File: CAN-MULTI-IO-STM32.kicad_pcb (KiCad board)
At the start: 2 copper layers, 81 x 55 mm, 63 parts, among them J1 H GND L, J2 TERM, J3 USART1, J5 PWR IN, U1 STM32L433RCT3, U2 MCP2562-E-SN, U3 LMR54410, U4 ADS1015IDGS, U5 PCA9537, U6 TCA9511

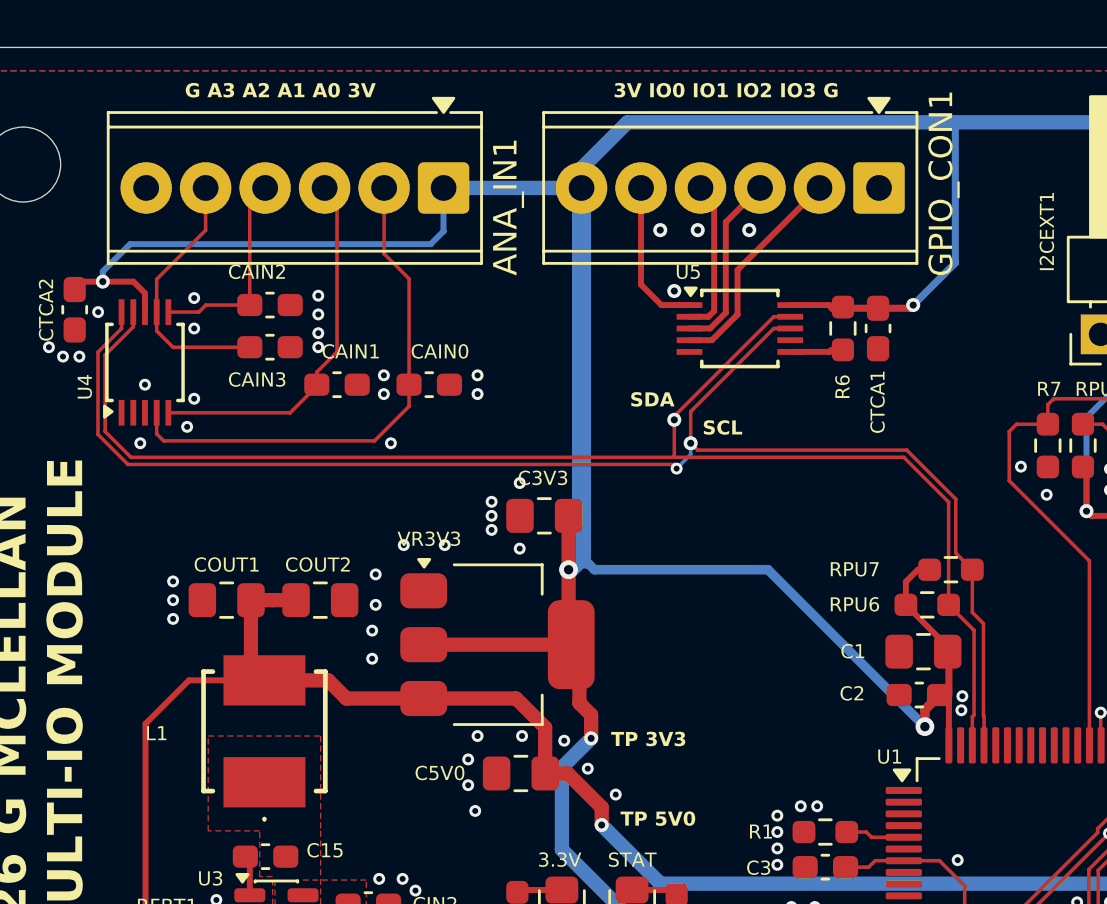
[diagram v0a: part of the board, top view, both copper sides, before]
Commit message: fix 2.54mm terminal block issues
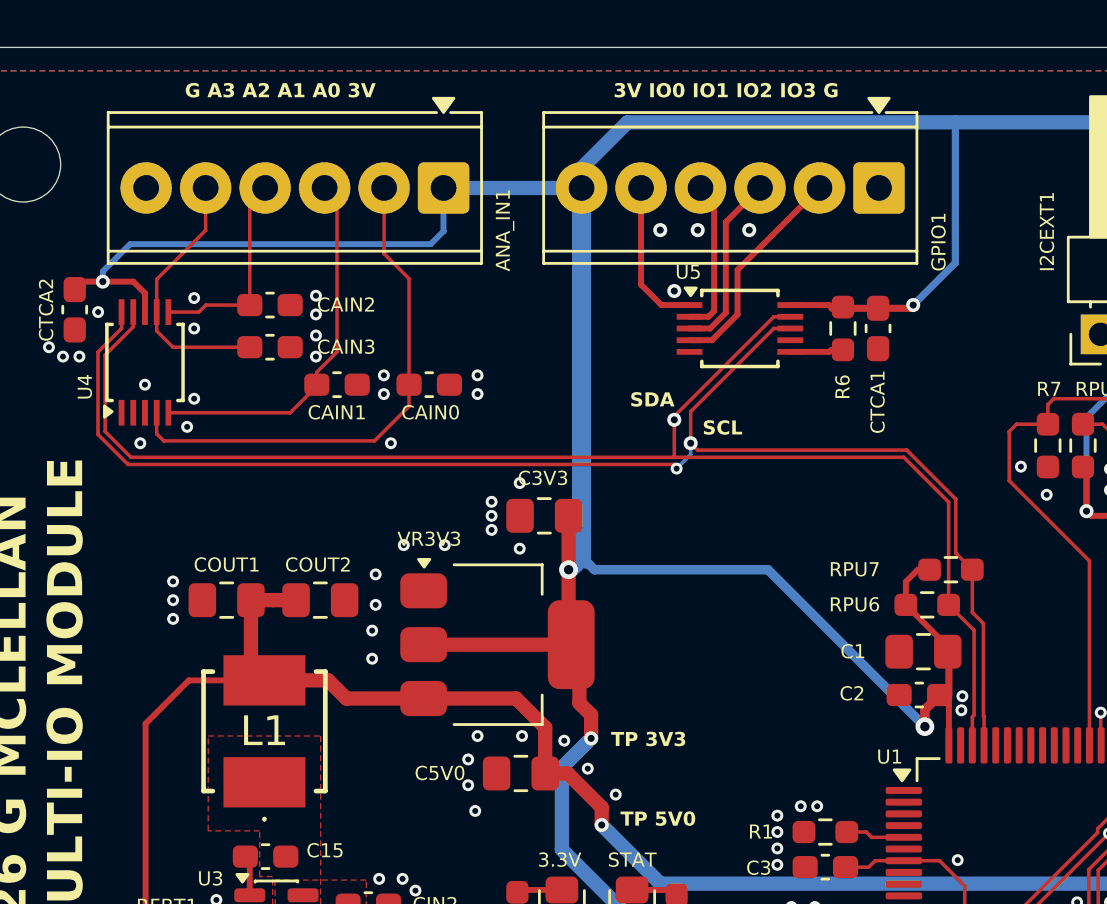
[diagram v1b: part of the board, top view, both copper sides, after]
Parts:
- ANA_IN1: value Conn_01x06 -> 1725698
- GPIO1: renamed from GPIO_CON1; value Conn_01x06 -> 1725698
- L1: value SRP5030HMT-8R2M -> 8.2 uH 55.2 mOhm
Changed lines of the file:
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@@
 	(net 65 "/I2C1_SDA")
 	(net 66 "/I2C1_SCL")
-	(net 67 "Net-(GPIO_CON1-Pin_3)")
-	(net 68 "Net-(GPIO_CON1-Pin_5)")
-	(net 69 "Net-(GPIO_CON1-Pin_2)")
-	(net 70 "Net-(GPIO_CON1-Pin_4)")
+	(net 67 "Net-(GPIO1-Pin_3)")
+	(net 68 "Net-(GPIO1-Pin_5)")
+	(net 69 "Net-(GPIO1-Pin_2)")
+	(net 70 "Net-(GPIO1-Pin_4)")
 	(net 71 "Net-(U5-~{RESET})")
 	(net 72 "unconnected-(U5-~{INT}-Pad7)")
@@
 		(tags "capacitor handsolder")
 		(property "Reference" "CAIN2"
-			(at -0.5375 -1.4 0)
+			(at 3.2625 0 0)
 			(layer "F.SilkS")
 			(effects
@@
 			(size 1.1 0.25)
 			(layers "F.Cu" "F.Mask" "F.Paste")
-			(net 68 "Net-(GPIO_CON1-Pin_5)")
+			(net 68 "Net-(GPIO1-Pin_5)")
 			(pinfunction "IO0")
 			(pintype "bidirectional")
@@
 			(size 1.1 0.25)
 			(layers "F.Cu" "F.Mask" "F.Paste")
-			(net 70 "Net-(GPIO_CON1-Pin_4)")
+			(net 70 "Net-(GPIO1-Pin_4)")
 			(pinfunction "IO1")
 			(pintype "bidirectional")
@@
 			(size 1.1 0.25)
 			(layers "F.Cu" "F.Mask" "F.Paste")
-			(net 67 "Net-(GPIO_CON1-Pin_3)")
+			(net 67 "Net-(GPIO1-Pin_3)")
 			(pinfunction "IO2")
 			(pintype "bidirectional")
@@
 			(size 1.1 0.25)
 			(layers "F.Cu" "F.Mask" "F.Paste")
-			(net 69 "Net-(GPIO_CON1-Pin_2)")
+			(net 69 "Net-(GPIO1-Pin_2)")
 			(pinfunction "IO3")
 			(pintype "bidirectional")
@@
 		(tags "capacitor handsolder")
 		(property "Reference" "CAIN3"
-			(at -0.5375 1.4 0)
+			(at 3.2625 0 0)
 			(layer "F.SilkS")
 			(effects
@@
 		(descr "Terminal Block Phoenix MPT-0,5-6-2.54, 6 pins, pitch 2.54mm, size 15.7x6.2mm, drill diameter 1.1mm, pad diameter 2.2mm, http://www.mouser.com/ds/2/324/ItemDetail_1725672-916605.pdf, script-generated using https://gitlab.com/kicad/libraries/kicad-footprint-generator/-/tree/master/scripts/TerminalBlock_Phoenix")
 		(tags "THT Terminal Block Phoenix MPT-0,5-6-2.54 pitch 2.54mm size 15.7x6.2mm drill 1.1mm pad 2.2mm")
-		(property "Reference" "GPIO_CON1"
-			(at -2.66 0.2 270)
+		(property "Reference" "GPIO1"
+			(at -2.56 -2.3 270)
 			(layer "F.SilkS")
 			(effects
 				(font
-					(size 1 1)
-					(thickness 0.15)
+					(size 0.6 0.6)
+					(thickness 0.1)
 				)
 			)
 		)
-		(property "Value" "Conn_01x06"
+		(property "Value" "1725698"
 			(at 6.35 4.22 180)
 			(layer "F.Fab")
@@
 			)
 		)
-		(property "Datasheet" "~"
+		(property "Datasheet" "https://www.mouser.com/datasheet/3/507/9/phoenix_contact_1725698_en.pdf"
 			(at 0 0 180)
 			(layer "F.Fab")
@@
 			)
 		)
-		(property "Description" "Generic connector, single row, 01x06, script generated (kicad-library-utils/schlib/autogen/connector/)"
+		(property "Description" "Phoenix Contact 1725698"
 			(at 0 0 180)
 			(layer "F.Fab")
@@
 			(layers "*.Cu" "*.Mask")
 			(remove_unused_layers no)
-			(net 69 "Net-(GPIO_CON1-Pin_2)")
+			(net 69 "Net-(GPIO1-Pin_2)")
 			(pinfunction "Pin_2")
 			(pintype "passive")
@@
 			(layers "*.Cu" "*.Mask")
 			(remove_unused_layers no)
-			(net 67 "Net-(GPIO_CON1-Pin_3)")
+			(net 67 "Net-(GPIO1-Pin_3)")
 			(pinfunction "Pin_3")
 			(pintype "passive")
@@
 			(layers "*.Cu" "*.Mask")
 			(remove_unused_layers no)
-			(net 70 "Net-(GPIO_CON1-Pin_4)")
+			(net 70 "Net-(GPIO1-Pin_4)")
 			(pinfunction "Pin_4")
 			(pintype "passive")
@@
 			(layers "*.Cu" "*.Mask")
 			(remove_unused_layers no)
-			(net 68 "Net-(GPIO_CON1-Pin_5)")
+			(net 68 "Net-(GPIO1-Pin_5)")
 			(pinfunction "Pin_5")
 			(pintype "passive")
@@
 		(tags "capacitor handsolder")
 		(property "Reference" "CAIN0"
-			(at 0.4625 -1.4 0)
+			(at 0.0625 1.2 0)
 			(layer "F.SilkS")
 			(effects
@@
 		(tags "THT Terminal Block Phoenix MPT-0,5-6-2.54 pitch 2.54mm size 15.7x6.2mm drill 1.1mm pad 2.2mm")
 		(property "Reference" "ANA_IN1"
-			(at -2.65 -0.8 270)
+			(at -2.55 -1.8 270)
 			(layer "F.SilkS")
 			(effects
 				(font
-					(size 1 1)
-					(thickness 0.15)
+					(size 0.6 0.6)
+					(thickness 0.1)
 				)
 			)
 		)
-		(property "Value" "Conn_01x06"
+		(property "Value" "1725698"
 			(at 6.35 4.22 180)
 			(layer "F.Fab")
@@
 			)
 		)
-		(property "Datasheet" "~"
+		(property "Datasheet" "https://www.mouser.com/datasheet/3/507/9/phoenix_contact_1725698_en.pdf"
 			(at 0 0 180)
 			(layer "F.Fab")
@@
 			)
 		)
-		(property "Description" "Generic connector, single row, 01x06, script generated (kicad-library-utils/schlib/autogen/connector/)"
+		(property "Description" "Phoenix Contact 1725698"
 			(at 0 0 180)
 			(layer "F.Fab")
@@
 		(tags "Inductor")
 		(property "Reference" "L1"
-			(at -4.6 0.1 0)
+			(at 0 0 0)
 			(layer "F.SilkS")
 			(effects
 				(font
-					(size 0.6 0.6)
-					(thickness 0.1)
+					(size 1.27 1.27)
+					(thickness 0.254)
 				)
 			)
 		)
-		(property "Value" "SRP5030HMT-8R2M"
+		(property "Value" "8.2 uH 55.2 mOhm"
 			(at 0 0 0)
 			(layer "F.SilkS")
@@
 			)
 		)
-		(property "Mouser Part Number" ""
+		(property "Mouser Part Number" "SRP5030HMT-8R2M"
 			(at 0 0 0)
 			(unlocked yes)
@@
 		(tags "capacitor handsolder")
 		(property "Reference" "CAIN1"
-			(at 0.6 -1.4 0)
+			(at 0 1.2 0)
 			(layer "F.SilkS")
 			(effects
@@
 	)
 	(via
-		(at 113.6 87.8)
+		(at 113.5 88.2)
 		(size 0.508)
 		(drill 0.254)
@@
 	)
 	(via
-		(at 113.6 85.6)
+		(at 113.5 85.6)
 		(size 0.508)
 		(drill 0.254)
@@
 	)
 	(via
-		(at 113.6 86.4)
+		(at 113.5 86.4)
 		(size 0.508)
 		(drill 0.254)
@@
 	)
 	(via
-		(at 113.6 87.2)
+		(at 113.5 87.3)
 		(size 0.508)
 		(drill 0.254)

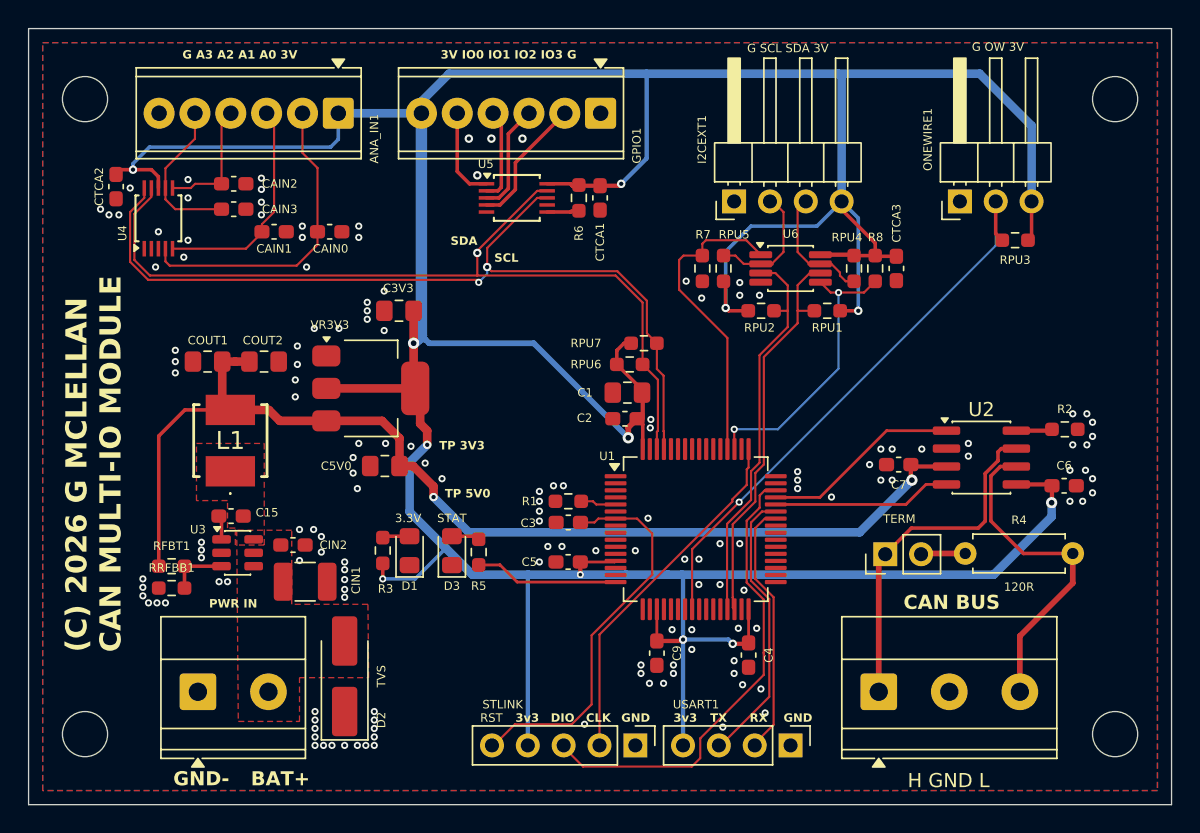
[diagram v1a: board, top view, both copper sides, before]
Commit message: fix a few footprint and drc issues
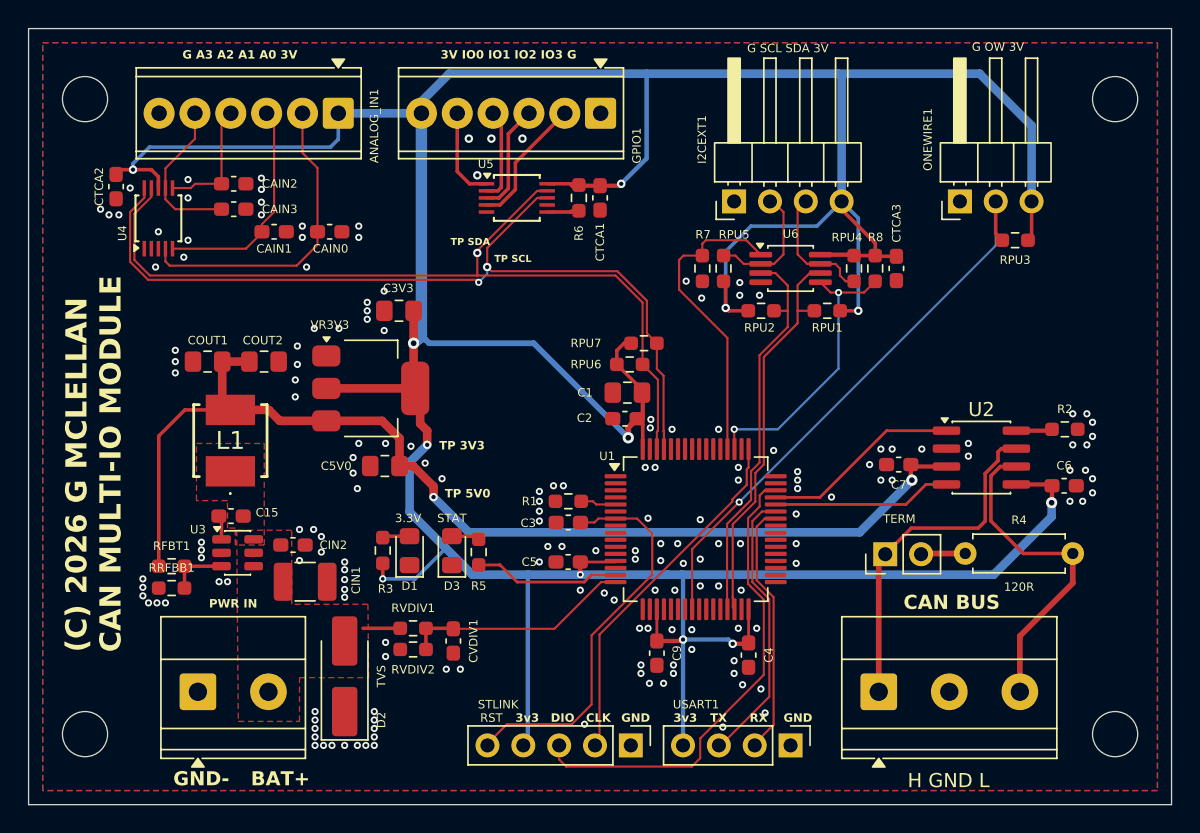
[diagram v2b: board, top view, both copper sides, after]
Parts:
- added CVDIV1: 100n, Capacitor_SMD:C_0603_1608Metric_Pad1.08x0.95mm_HandSolder, F.Cu at (127.1, 118.4)
- added RVDIV1: 4K7, Resistor_SMD:R_0603_1608Metric_Pad0.98x0.95mm_HandSolder, F.Cu at (124.2, 117.5)
- added RVDIV2: 1K0, Resistor_SMD:R_0603_1608Metric_Pad0.98x0.95mm_HandSolder, F.Cu at (124.2, 119.0)
- U6: value TCA9511 -> PI6ULS5V9511AUEX; footprint Package_SO:VSSOP-8_3x3mm_P0.65mm -> Package_SO:MSOP-8_3x3mm_P0.65mm
- moved SWD1 0.32 mm to (139.7, 125.8)
- renumbered ANA_IN1 to ANALOG_IN1
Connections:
- U1 pad 15: unconnected-(U1-PA1-Pad15) -> /STATUS
- U1 pad 16: /STATUS -> /VDIV
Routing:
- net /VDIV: track 0.00 -> 16.3 mm
- net +3.3V: track 308.3 -> 304.2 mm
- net +12V: track 0.35 -> 2.64 mm
- net /AIN1: track 16.8 -> 15.0 mm
- net +5V: track 79.4 -> 78.4 mm
- net /AIN2: track 8.87 -> 7.94 mm
- net Net-(GPIO1-Pin_4): track 6.65 -> 5.83 mm
- net /SWDIO: track 33.3 -> 34.0 mm
- net /CANH: track 24.7 -> 24.0 mm
- net GND: vias 149 -> 175
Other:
- board text added: "TP SCL"
- board text added: "TP SDA"
- board text removed: "SCL"
- board text removed: "SDA"

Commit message: rename gpio header
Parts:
- renumbered GPIO1 to DIGITAL_IO1
